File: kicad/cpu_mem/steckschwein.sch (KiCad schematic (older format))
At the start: 32 parts, among them P1 CONN_02X04, P3 CONN_01X03, P4 CONN_02X02, SW1 SW_PUSH, U1 W65C02SP, U2 LM555N, U3 74HCT00, U4 74LS393, U5 GAL22V10, U6 28C256, U7 HM62256BLP-7, U8 HM62256BLP-7, U9 74LS139, X1 OSC

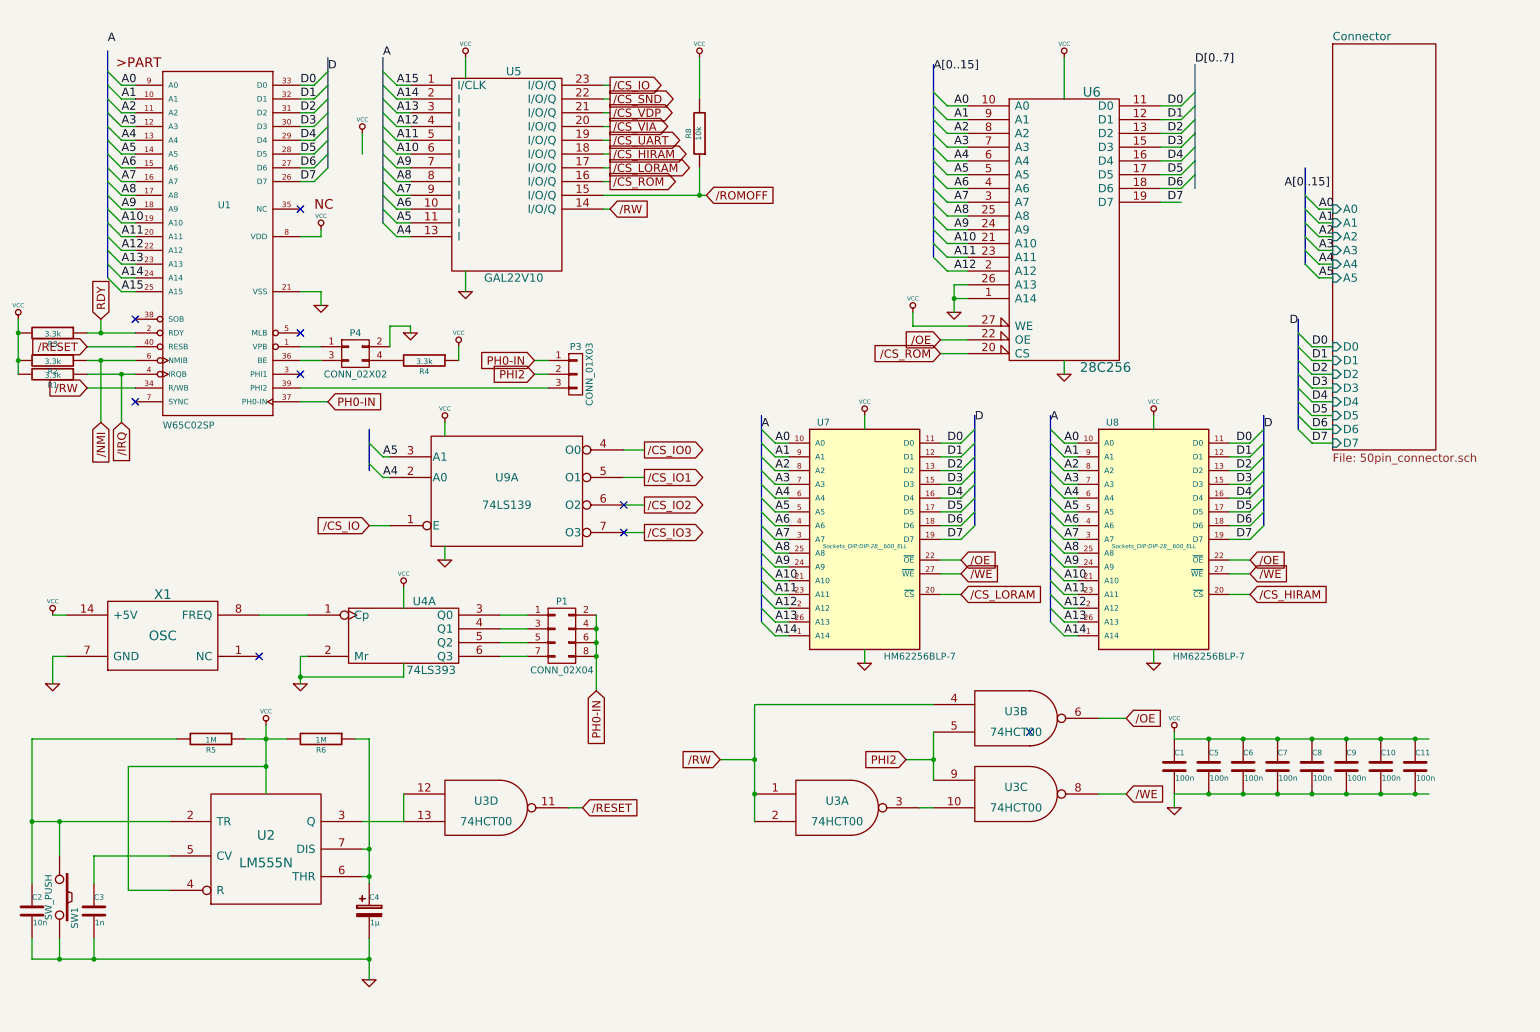
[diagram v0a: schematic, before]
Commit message: decoder w. latch, own module
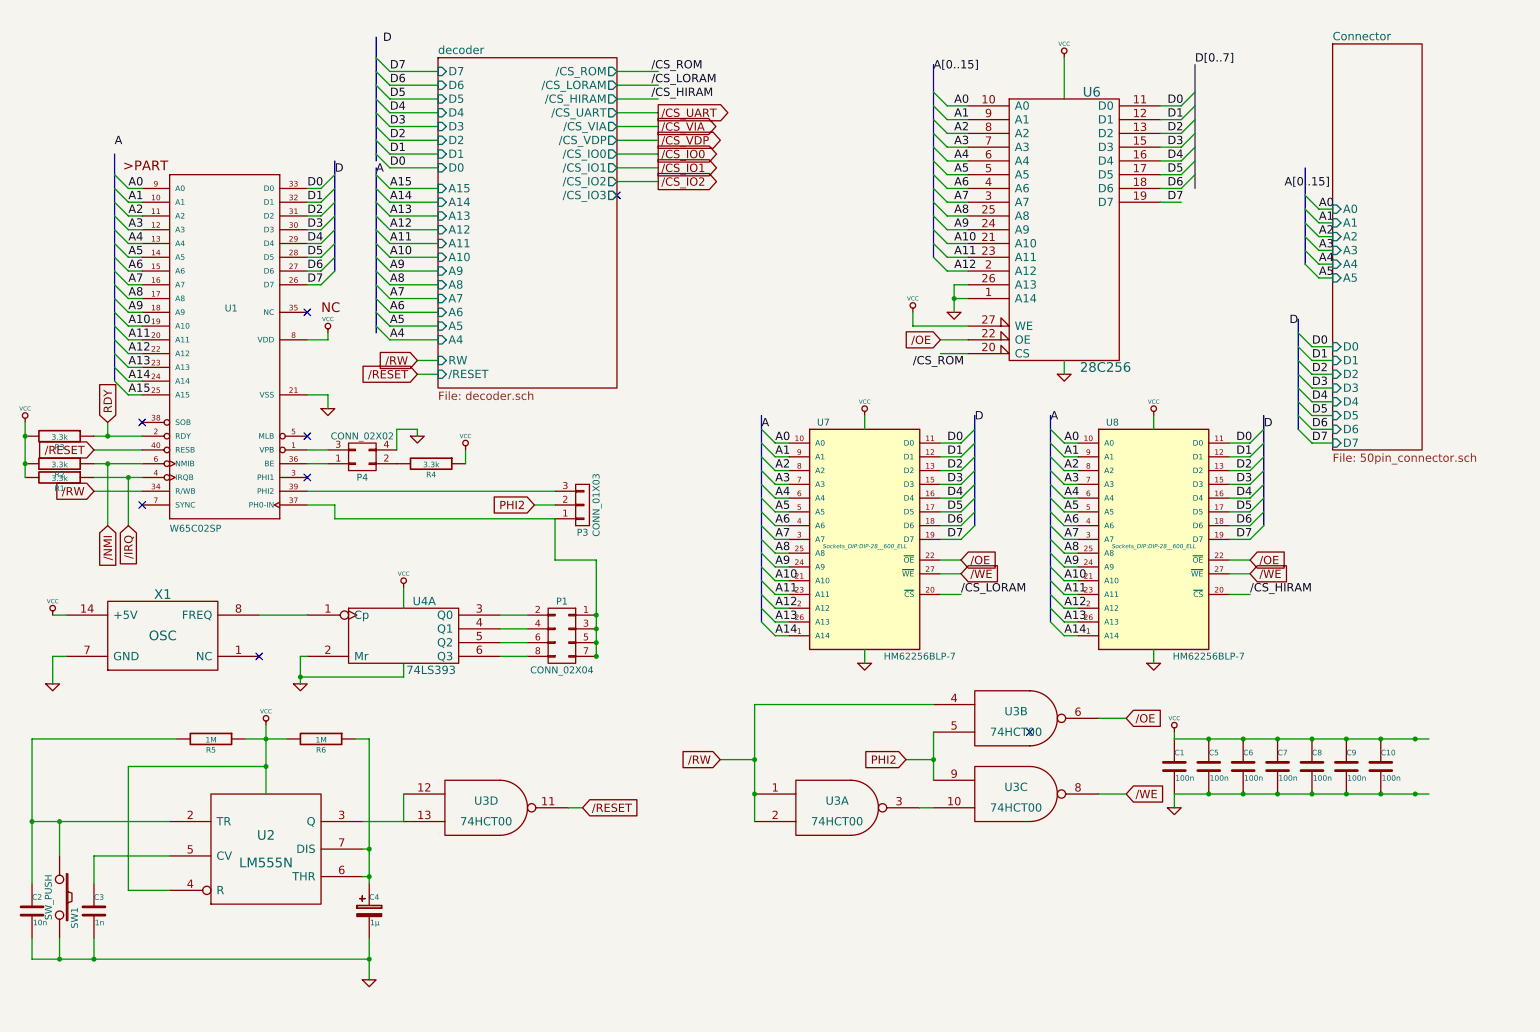
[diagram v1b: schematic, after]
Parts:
- removed C11: 100n, Discret:C1, symbol C
- removed R8: 10k, Discret:R3, symbol R
- removed U5: GAL22V10, Sockets_DIP:DIP-24__300_ELL, symbol GAL22V10
- removed U9: 74LS139, Sockets_DIP:DIP-14__300_ELL, symbol 74LS139
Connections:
- net /CS_ROM: no longer U6.20 (CS)
- net GND: now also P4.4 (P4); no longer P4.2 (P2)
- net at U1.1 (VPB): now also P4.3 (P3); no longer P4.1 (P1)
- net at U1.36 (BE): now also P4.1 (P1); no longer P4.3 (P3)
- net at R4.2: now also P4.2 (P2); no longer P4.4 (P4)
- net at P1.1 (P1): now also P1.3 (P3), P1.5 (P5), P1.7 (P7), P3.1 (P1), U1.37 (PH0-IN); no longer U4.3 (Q0)
- net at U4.4 (Q1): now also P1.4 (P4); no longer P1.3 (P3)
- net at U4.5 (Q2): now also P1.6 (P6); no longer P1.5 (P5)
- net at U4.6 (Q3): now also P1.8 (P8); no longer P1.7 (P7)
- removed net PH0-IN: P1.2 (P2), P1.4 (P4), P1.6 (P6), P1.8 (P8), P3.1 (P1), U1.37 (PH0-IN)
- new net: P1.2 (P2), U4.3 (Q0)
- no-connect marks 9 -> 8
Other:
- moved on the sheet: P3, P4, R1, R2, R3, R4, U1

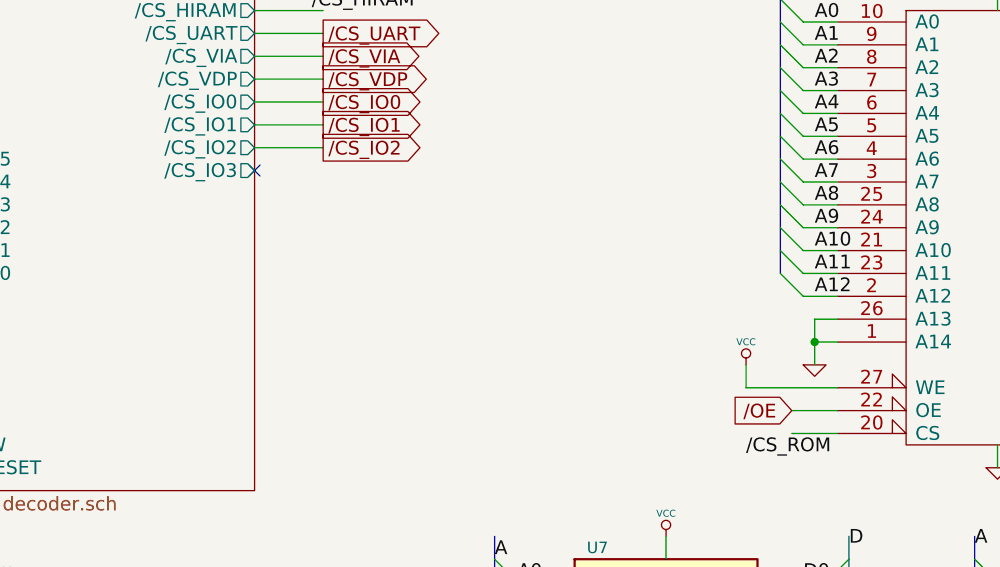
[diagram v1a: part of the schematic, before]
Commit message: rom banking pins
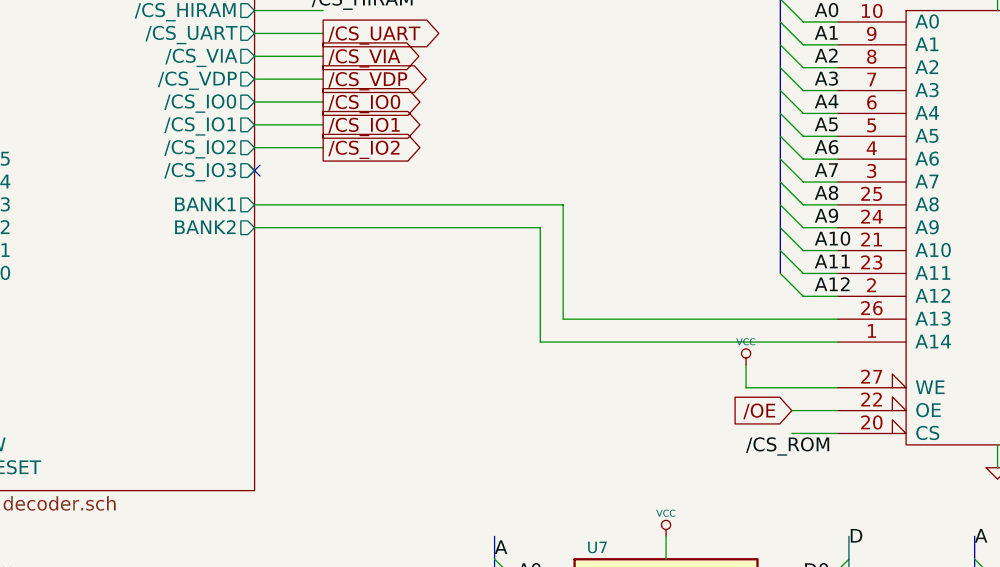
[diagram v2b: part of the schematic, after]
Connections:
- net GND: no longer U6.1 (A14), U6.26 (A13)
- new net decoder/BANK1: U6.26 (A13)
- new net decoder/BANK2: U6.1 (A14)
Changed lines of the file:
@@
 LIBS:74xgxx
 LIBS:ttl_ieee
-LIBS:steckschwein-cache
 EELAYER 24 0
 EELAYER END
@@
 $EndComp
 $Comp
-L VCC #PWR01
+L VCC #PWR20
 U 1 1 5413678B
 P 8900 5600
-F 0 "#PWR01" H 8900 5700 30  0001 C CNN
+F 0 "#PWR20" H 8900 5700 30  0001 C CNN
 F 1 "VCC" H 8900 5700 30  0000 C CNN
 F 2 "" H 8900 5600 60  0000 C CNN
@@
 $EndComp
 $Comp
-L GND #PWR02
+L GND #PWR21
 U 1 1 541367AD
 P 8900 6150
-F 0 "#PWR02" H 8900 6150 30  0001 C CNN
+F 0 "#PWR21" H 8900 6150 30  0001 C CNN
 F 1 "GND" H 8900 6080 30  0001 C CNN
 F 2 "" H 8900 6150 60  0000 C CNN
@@
 $EndComp
 $Comp
-L VCC #PWR03
+L VCC #PWR6
 U 1 1 54136970
 P 2750 2700
-F 0 "#PWR03" H 2750 2800 30  0001 C CNN
+F 0 "#PWR6" H 2750 2800 30  0001 C CNN
 F 1 "VCC" H 2750 2800 30  0000 C CNN
 F 2 "" H 2750 2700 60  0000 C CNN
@@
 $EndComp
 $Comp
-L GND #PWR04
+L GND #PWR7
 U 1 1 541369C9
 P 2750 3250
-F 0 "#PWR04" H 2750 3250 30  0001 C CNN
+F 0 "#PWR7" H 2750 3250 30  0001 C CNN
 F 1 "GND" H 2750 3180 30  0001 C CNN
 F 2 "" H 2750 3250 60  0000 C CNN
@@
 $EndComp
 $Comp
-L VCC #PWR05
+L VCC #PWR4
 U 1 1 54136DD8
 P 2300 5550
-F 0 "#PWR05" H 2300 5650 30  0001 C CNN
+F 0 "#PWR4" H 2300 5650 30  0001 C CNN
 F 1 "VCC" H 2300 5650 30  0000 C CNN
 F 2 "" H 2300 5550 60  0000 C CNN
@@
 $EndComp
 $Comp
-L GND #PWR06
+L GND #PWR8
 U 1 1 541371BF
 P 3050 7400
-F 0 "#PWR06" H 3050 7400 30  0001 C CNN
+F 0 "#PWR8" H 3050 7400 30  0001 C CNN
 F 1 "GND" H 3050 7330 30  0001 C CNN
 F 2 "" H 3050 7400 60  0000 C CNN
@@
 $EndComp
 $Comp
-L VCC #PWR07
+L VCC #PWR1
 U 1 1 5413551C
 P 550 3350
-F 0 "#PWR07" H 550 3450 30  0001 C CNN
+F 0 "#PWR1" H 550 3450 30  0001 C CNN
 F 1 "VCC" H 550 3450 30  0000 C CNN
 F 2 "" H 550 3350 60  0000 C CNN
@@
 $EndComp
 $Comp
-L VCC #PWR08
+L VCC #PWR11
 U 1 1 5413558F
 P 3750 3550
-F 0 "#PWR08" H 3750 3650 30  0001 C CNN
+F 0 "#PWR11" H 3750 3650 30  0001 C CNN
 F 1 "VCC" H 3750 3650 30  0000 C CNN
 F 2 "" H 3750 3550 60  0000 C CNN
@@
 $EndComp
 $Comp
-L VCC #PWR09
+L VCC #PWR2
 U 1 1 54136377
 P 750 4750
-F 0 "#PWR09" H 750 4850 30  0001 C CNN
+F 0 "#PWR2" H 750 4850 30  0001 C CNN
 F 1 "VCC" H 750 4850 30  0000 C CNN
 F 2 "" H 750 4750 60  0000 C CNN
@@
 $EndComp
 $Comp
-L GND #PWR010
+L GND #PWR3
 U 1 1 541363D2
 P 750 5250
-F 0 "#PWR010" H 750 5250 30  0001 C CNN
+F 0 "#PWR3" H 750 5250 30  0001 C CNN
 F 1 "GND" H 750 5180 30  0001 C CNN
 F 2 "" H 750 5250 60  0000 C CNN
@@
 $EndComp
 $Comp
-L GND #PWR011
+L GND #PWR5
 U 1 1 5413653F
 P 2550 5250
-F 0 "#PWR011" H 2550 5250 30  0001 C CNN
+F 0 "#PWR5" H 2550 5250 30  0001 C CNN
 F 1 "GND" H 2550 5180 30  0001 C CNN
 F 2 "" H 2550 5250 60  0000 C CNN
@@
 $EndComp
 $Comp
-L VCC #PWR012
+L VCC #PWR9
 U 1 1 5413674B
 P 3300 4550
-F 0 "#PWR012" H 3300 4650 30  0001 C CNN
+F 0 "#PWR9" H 3300 4650 30  0001 C CNN
 F 1 "VCC" H 3300 4650 30  0000 C CNN
 F 2 "" H 3300 4550 60  0000 C CNN
@@
 $EndComp
 $Comp
-L VCC #PWR013
+L VCC #PWR14
 U 1 1 5413EA26
 P 7000 2550
-F 0 "#PWR013" H 7000 2650 30  0001 C CNN
+F 0 "#PWR14" H 7000 2650 30  0001 C CNN
 F 1 "VCC" H 7000 2650 30  0000 C CNN
 F 2 "" H 7000 2550 60  0000 C CNN
@@
 $EndComp
 $Comp
-L GND #PWR014
+L GND #PWR10
 U 1 1 5414A44F
 P 3400 3450
-F 0 "#PWR014" H 3400 3450 30  0001 C CNN
+F 0 "#PWR10" H 3400 3450 30  0001 C CNN
 F 1 "GND" H 3400 3380 30  0001 C CNN
 F 2 "" H 3400 3450 60  0000 C CNN
@@
 Text GLabel 1150 3350 1    60   Input ~ 0
 RDY
-$Comp
-L GND #PWR015
-U 1 1 54357F26
-P 7300 2550
-F 0 "#PWR015" H 7300 2550 30  0001 C CNN
-F 1 "GND" H 7300 2480 30  0001 C CNN
-F 2 "" H 7300 2550 60  0000 C CNN
-F 3 "" H 7300 2550 60  0000 C CNN
-	1    7300 2550
-	1    0    0    -1
-$EndComp
 Entry Wire Line
 	9850 2200 9950 2300
@@
 A5
 $Comp
-L VCC #PWR016
+L VCC #PWR16
 U 1 1 543745A2
 P 8100 700
-F 0 "#PWR016" H 8100 800 30  0001 C CNN
+F 0 "#PWR16" H 8100 800 30  0001 C CNN
 F 1 "VCC" H 8100 800 30  0000 C CNN
 F 2 "" H 8100 700 60  0000 C CNN
@@
 $EndComp
 $Comp
-L GND #PWR017
+L GND #PWR17
 U 1 1 543748B3
 P 8100 3000
-F 0 "#PWR017" H 8100 3000 30  0001 C CNN
+F 0 "#PWR17" H 8100 3000 30  0001 C CNN
 F 1 "GND" H 8100 2930 30  0001 C CNN
 F 2 "" H 8100 3000 60  0000 C CNN
@@
 $EndComp
 $Comp
-L VCC #PWR018
+L VCC #PWR12
 U 1 1 54374D46
 P 6650 3300
-F 0 "#PWR018" H 6650 3400 30  0001 C CNN
+F 0 "#PWR12" H 6650 3400 30  0001 C CNN
 F 1 "VCC" H 6650 3400 30  0000 C CNN
 F 2 "" H 6650 3300 60  0000 C CNN
@@
 $EndComp
 $Comp
-L VCC #PWR019
+L VCC #PWR18
 U 1 1 54374E0E
 P 8750 3300
-F 0 "#PWR019" H 8750 3400 30  0001 C CNN
+F 0 "#PWR18" H 8750 3400 30  0001 C CNN
 F 1 "VCC" H 8750 3400 30  0000 C CNN
 F 2 "" H 8750 3300 60  0000 C CNN
@@
 $EndComp
 $Comp
-L GND #PWR020
+L GND #PWR13
 U 1 1 54375105
 P 6650 5100
-F 0 "#PWR020" H 6650 5100 30  0001 C CNN
+F 0 "#PWR13" H 6650 5100 30  0001 C CNN
 F 1 "GND" H 6650 5030 30  0001 C CNN
 F 2 "" H 6650 5100 60  0000 C CNN
@@
 $EndComp
 $Comp
-L GND #PWR021
+L GND #PWR19
 U 1 1 54375267
 P 8750 5100
-F 0 "#PWR021" H 8750 5100 30  0001 C CNN
+F 0 "#PWR19" H 8750 5100 30  0001 C CNN
 F 1 "GND" H 8750 5030 30  0001 C CNN
 F 2 "" H 8750 5100 60  0000 C CNN
@@
 F32 "/CS_IO3" O R 4850 1700 60
 F33 "/RESET" I L 3550 3000 60
+F34 "BANK1" O R 4850 1850 60
+F35 "BANK2" O R 4850 1950 60
 $EndSheet
 Text GLabel 3400 2900 0    60   Input ~ 0
@@
 Connection ~ 1150 3450
 Connection ~ 5850 6050
-Wire Wire Line
-	7400 2350 7300 2350
-Wire Wire Line
-	7300 2350 7300 2550
-Wire Wire Line
-	7400 2450 7300 2450
-Connection ~ 7300 2450
 Wire Wire Line
 	7000 2550 7000 2650
@@
 Wire Wire Line
 	4700 4350 4700 5050
+Wire Wire Line
+	4850 1850 6200 1850
+Wire Wire Line
+	6200 1850 6200 2350
+Wire Wire Line
+	6200 2350 7400 2350
+Wire Wire Line
+	7400 2450 6100 2450
+Wire Wire Line
+	6100 2450 6100 1950
+Wire Wire Line
+	6100 1950 4850 1950
 $EndSCHEMATC
